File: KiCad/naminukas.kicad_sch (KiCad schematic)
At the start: 10 parts

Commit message: fix(pcb): better symbol for TPSM84A21MOJR
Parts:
- added U?: TPSM84A21MOJR, Texas_Instruments-MOJ0020A-0-0-*, symbol Buck (build-in caps):TPSM84A21MOJR
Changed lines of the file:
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@@
     (pin "Y2")
+  )
+  (symbol (lib_id "Buck (build-in caps):TPSM84A21MOJR") (at 31.75 139.7 0) (unit 1)
+    (in_bom yes) (on_board yes) (fields_autoplaced)
+    (property "Reference" "U?" (id 0) (at 52.07 132.08 0))
+    (property "Value" "TPSM84A21MOJR" (id 1) (at 52.07 134.62 0))
+    (property "Footprint" "Texas_Instruments-MOJ0020A-0-0-*" (id 2) (at 31.75 129.54 0)
+      (effects (font (size 1.27 1.27)) (justify left) hide)
+    )
+    (property "Datasheet" "https://www.ti.com/lit/ds/symlink/tpsm84a21.pdf?ts=1616475331887&ref_url=https%253A%252F%252Fwww.ti.com%252Fproduct%252FTPSM84A21%253FkeyMatch%253DTPSM84A21MOJR%2526tisearch%253Dsearch-everything%2526usecase%253DOPN" (id 3) (at 31.75 127 0)
+      (effects (font (size 1.27 1.27)) (justify left) hide)
+    )
+    (property "ambient temperature range high" "+85°C" (id 4) (at 31.75 124.46 0)
+      (effects (font (size 1.27 1.27)) (justify left) hide)
+    )
+    (property "ambient temperature range low" "-40°C" (id 5) (at 31.75 121.92 0)
+      (effects (font (size 1.27 1.27)) (justify left) hide)
+    )
+    (property "automotive" "No" (id 6) (at 31.75 119.38 0)
+      (effects (font (size 1.27 1.27)) (justify left) hide)
+    )
+    (property "category" "IC" (id 7) (at 31.75 116.84 0)
+      (effects (font (size 1.27 1.27)) (justify left) hide)
+    )
+    (property "device class L1" "Integrated Circuits (ICs)" (id 8) (at 31.75 114.3 0)
+      (effects (font (size 1.27 1.27)) (justify left) hide)
+    )
+    (property "device class L2" "Power Management ICs" (id 9) (at 31.75 111.76 0)
+      (effects (font (size 1.27 1.27)) (justify left) hide)
+    )
+    (property "device class L3" "Voltage Regulators - Switching" (id 10) (at 31.75 109.22 0)
+      (effects (font (size 1.27 1.27)) (justify left) hide)
+    )
+    (property "digikey description" "DC DC CONVERTER 0.55-1.35V" (id 11) (at 31.75 106.68 0)
+      (effects (font (size 1.27 1.27)) (justify left) hide)
+    )
+    (property "digikey part number" "296-48785-1-ND" (id 12) (at 31.75 104.14 0)
+      (effects (font (size 1.27 1.27)) (justify left) hide)
+    )
+    (property "height" "2.3mm" (id 13) (at 31.75 101.6 0)
+      (effects (font (size 1.27 1.27)) (justify left) hide)
+    )
+    (property "ipc land pattern name" "CAPAD1016W80L630D240" (id 14) (at 31.75 99.06 0)
+      (effects (font (size 1.27 1.27)) (justify left) hide)
+    )
+    (property "lead free" "Yes" (id 15) (at 31.75 96.52 0)
+      (effects (font (size 1.27 1.27)) (justify left) hide)
+    )
+    (property "library id" "cebd5fe4464742bf" (id 16) (at 31.75 93.98 0)
+      (effects (font (size 1.27 1.27)) (justify left) hide)
+    )
+    (property "manufacturer" "Texas Instruments" (id 17) (at 31.75 91.44 0)
+      (effects (font (size 1.27 1.27)) (justify left) hide)
+    )
+    (property "max duty cycle" "80%" (id 18) (at 31.75 88.9 0)
+      (effects (font (size 1.27 1.27)) (justify left) hide)
+    )
+    (property "max junction temp" "+125°C" (id 19) (at 31.75 86.36 0)
+      (effects (font (size 1.27 1.27)) (justify left) hide)
+    )
+    (property "max supply voltage" "14V" (id 20) (at 31.75 83.82 0)
+      (effects (font (size 1.27 1.27)) (justify left) hide)
+    )
+    (property "min supply voltage" "8V" (id 21) (at 31.75 81.28 0)
+      (effects (font (size 1.27 1.27)) (justify left) hide)
+    )
+    (property "mouser description" "8V to 14V, 0.508V to 1.35V Output, 10A Power Module with Integrated Input and Output Capacitors 20-QFM -40 to 85" (id 22) (at 31.75 78.74 0)
+      (effects (font (size 1.27 1.27)) (justify left) hide)
+    )
+    (property "mouser part number" "595-TPSM84A21MOJR" (id 23) (at 31.75 76.2 0)
+      (effects (font (size 1.27 1.27)) (justify left) hide)
+    )
+    (property "nominal supply current" "8mA" (id 24) (at 31.75 73.66 0)
+      (effects (font (size 1.27 1.27)) (justify left) hide)
+    )
+    (property "number of outputs" "1" (id 25) (at 31.75 71.12 0)
+      (effects (font (size 1.27 1.27)) (justify left) hide)
+    )
+    (property "output current" "10A" (id 26) (at 31.75 68.58 0)
+      (effects (font (size 1.27 1.27)) (justify left) hide)
+    )
+    (property "output type" "AdjustableProgrammable" (id 27) (at 31.75 66.04 0)
+      (effects (font (size 1.27 1.27)) (justify left) hide)
+    )
+    (property "output voltage" "0.55-1.35V" (id 28) (at 31.75 63.5 0)
+      (effects (font (size 1.27 1.27)) (justify left) hide)
+    )
+    (property "package" "QFM20" (id 29) (at 31.75 60.96 0)
+      (effects (font (size 1.27 1.27)) (justify left) hide)
+    )
+    (property "rohs" "Yes" (id 30) (at 31.75 58.42 0)
+      (effects (font (size 1.27 1.27)) (justify left) hide)
+    )
+    (property "switching frequency" "4MHz" (id 31) (at 31.75 55.88 0)
+      (effects (font (size 1.27 1.27)) (justify left) hide)
+    )
+    (property "temperature range high" "+85°C" (id 32) (at 31.75 53.34 0)
+      (effects (font (size 1.27 1.27)) (justify left) hide)
+    )
+    (property "temperature range low" "-40°C" (id 33) (at 31.75 50.8 0)
+      (effects (font (size 1.27 1.27)) (justify left) hide)
+    )
+    (pin "1")
+    (pin "10")
+    (pin "11")
+    (pin "12")
+    (pin "13")
+    (pin "14")
+    (pin "15")
+    (pin "16")
+    (pin "17")
+    (pin "18")
+    (pin "19")
+    (pin "2")
+    (pin "20")
+    (pin "3")
+    (pin "4")
+    (pin "5")
+    (pin "6")
+    (pin "7")
+    (pin "8")
+    (pin "9")
   )
   (symbol (lib_id "FPGA_Lattice:LFE5U-85F-6BG381x") (at 70.9676 73.7108 0) (unit 3)
@@
       (reference "IC?") (unit 1) (value "LSF0204DYZPR") (footprint "BGA12C50P3X4_144X194X50")
     )
+    (path "/66b1abfc-a54e-42e9-baa0-69e7c5971dd2"
+      (reference "U?") (unit 1) (value "TPSM84A21MOJR") (footprint "Texas_Instruments-MOJ0020A-0-0-*")
+    )
     (path "/f35b2073-882e-4ac0-9440-1e7208b06a2e"

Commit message: fix(pcb): better footprint for TPS84320RUQR
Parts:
- added U?: TPS84320RUQR, RUQ_47, symbol Buck converter:TPS84320RUQR
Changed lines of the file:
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@@
+    (pin "9")
+  )
+  (symbol (lib_id "Buck converter:TPS84320RUQR") (at 95.25 134.62 0) (unit 1)
+    (in_bom yes) (on_board yes) (fields_autoplaced)
+    (property "Reference" "U?" (id 0) (at 120.65 123.19 0)
+      (effects (font (size 1.524 1.524)))
+    )
+    (property "Value" "TPS84320RUQR" (id 1) (at 120.65 127 0)
+      (effects (font (size 1.524 1.524)))
+    )
+    (property "Footprint" "RUQ_47" (id 2) (at 120.65 128.524 0)
+      (effects (font (size 1.524 1.524)) hide)
+    )
+    (property "Datasheet" "" (id 3) (at 95.25 134.62 0)
+      (effects (font (size 1.524 1.524)))
+    )
+    (pin "1")
+    (pin "10")
+    (pin "11")
+    (pin "12")
+    (pin "13")
+    (pin "14")
+    (pin "15")
+    (pin "16")
+    (pin "17")
+    (pin "18")
+    (pin "19")
+    (pin "2")
+    (pin "20")
+    (pin "21")
+    (pin "22")
+    (pin "23")
+    (pin "24")
+    (pin "25")
+    (pin "26")
+    (pin "27")
+    (pin "28")
+    (pin "29")
+    (pin "3")
+    (pin "30")
+    (pin "31")
+    (pin "32")
+    (pin "33")
+    (pin "34")
+    (pin "35")
+    (pin "36")
+    (pin "37")
+    (pin "38")
+    (pin "39")
+    (pin "4")
+    (pin "40")
+    (pin "41")
+    (pin "42")
+    (pin "43")
+    (pin "44")
+    (pin "45")
+    (pin "46")
+    (pin "47")
+    (pin "5")
+    (pin "6")
+    (pin "7")
+    (pin "8")
     (pin "9")
   )
@@
       (reference "U?") (unit 1) (value "TPSM84A21MOJR") (footprint "Texas_Instruments-MOJ0020A-0-0-*")
     )
+    (path "/70e86428-6b27-40a3-ae68-cb62b9e219e9"
+      (reference "U?") (unit 1) (value "TPS84320RUQR") (footprint "RUQ_47")
+    )
     (path "/f35b2073-882e-4ac0-9440-1e7208b06a2e"

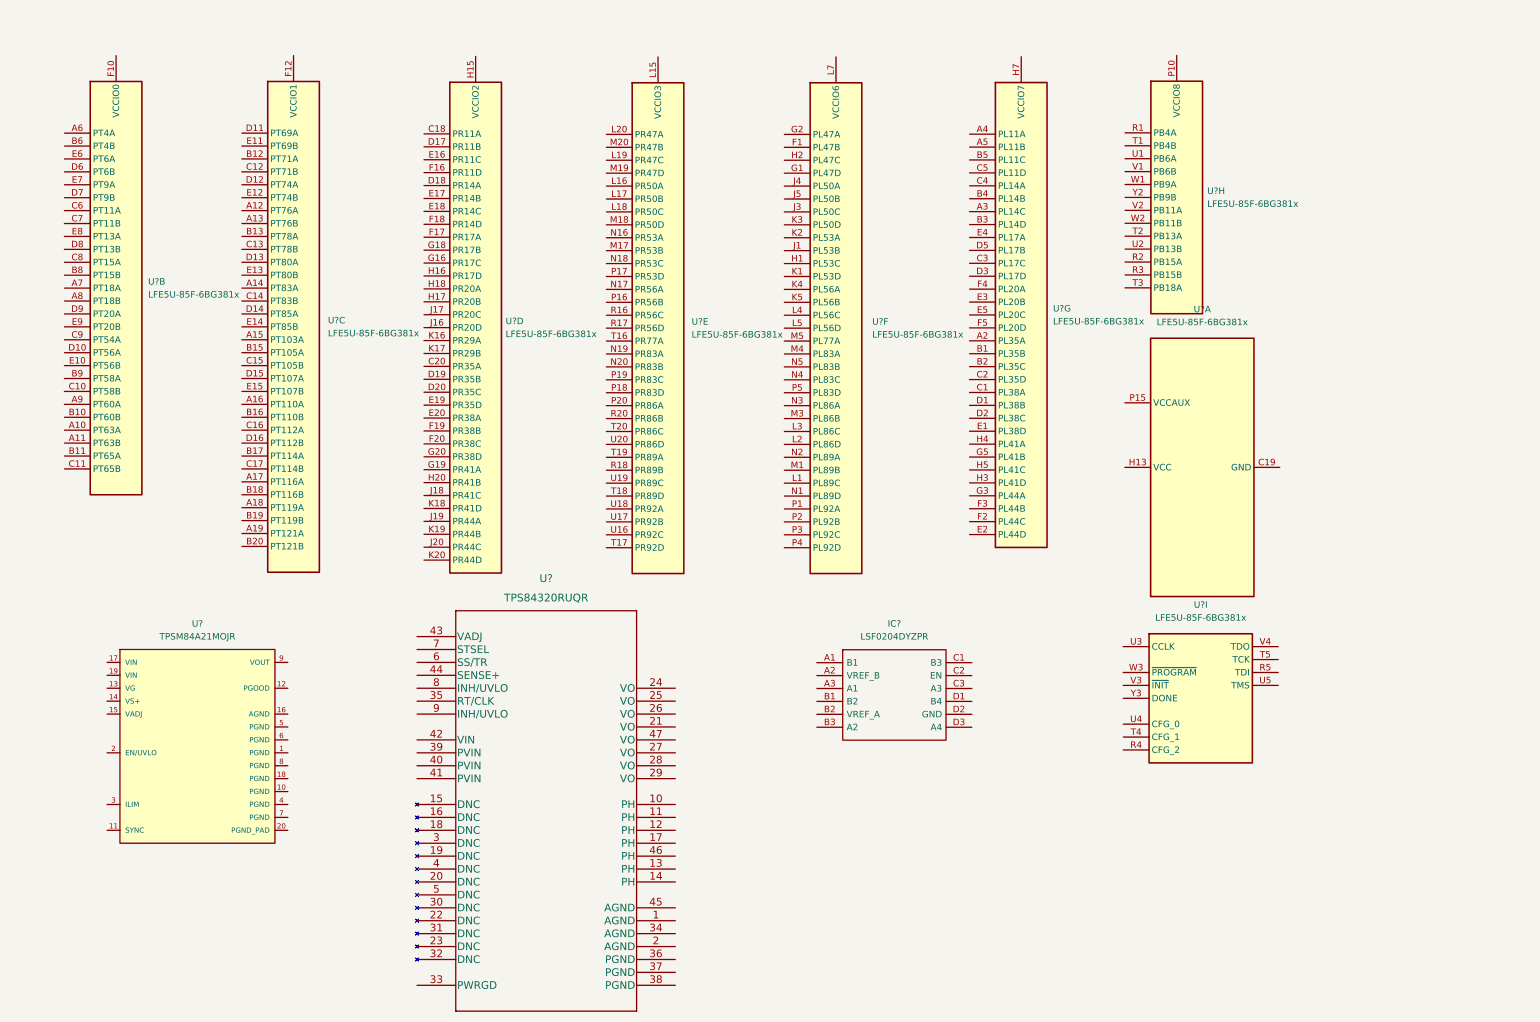
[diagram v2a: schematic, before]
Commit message: feat(pcb): add symbol/footprint for LFE5U-85F-6MG285C
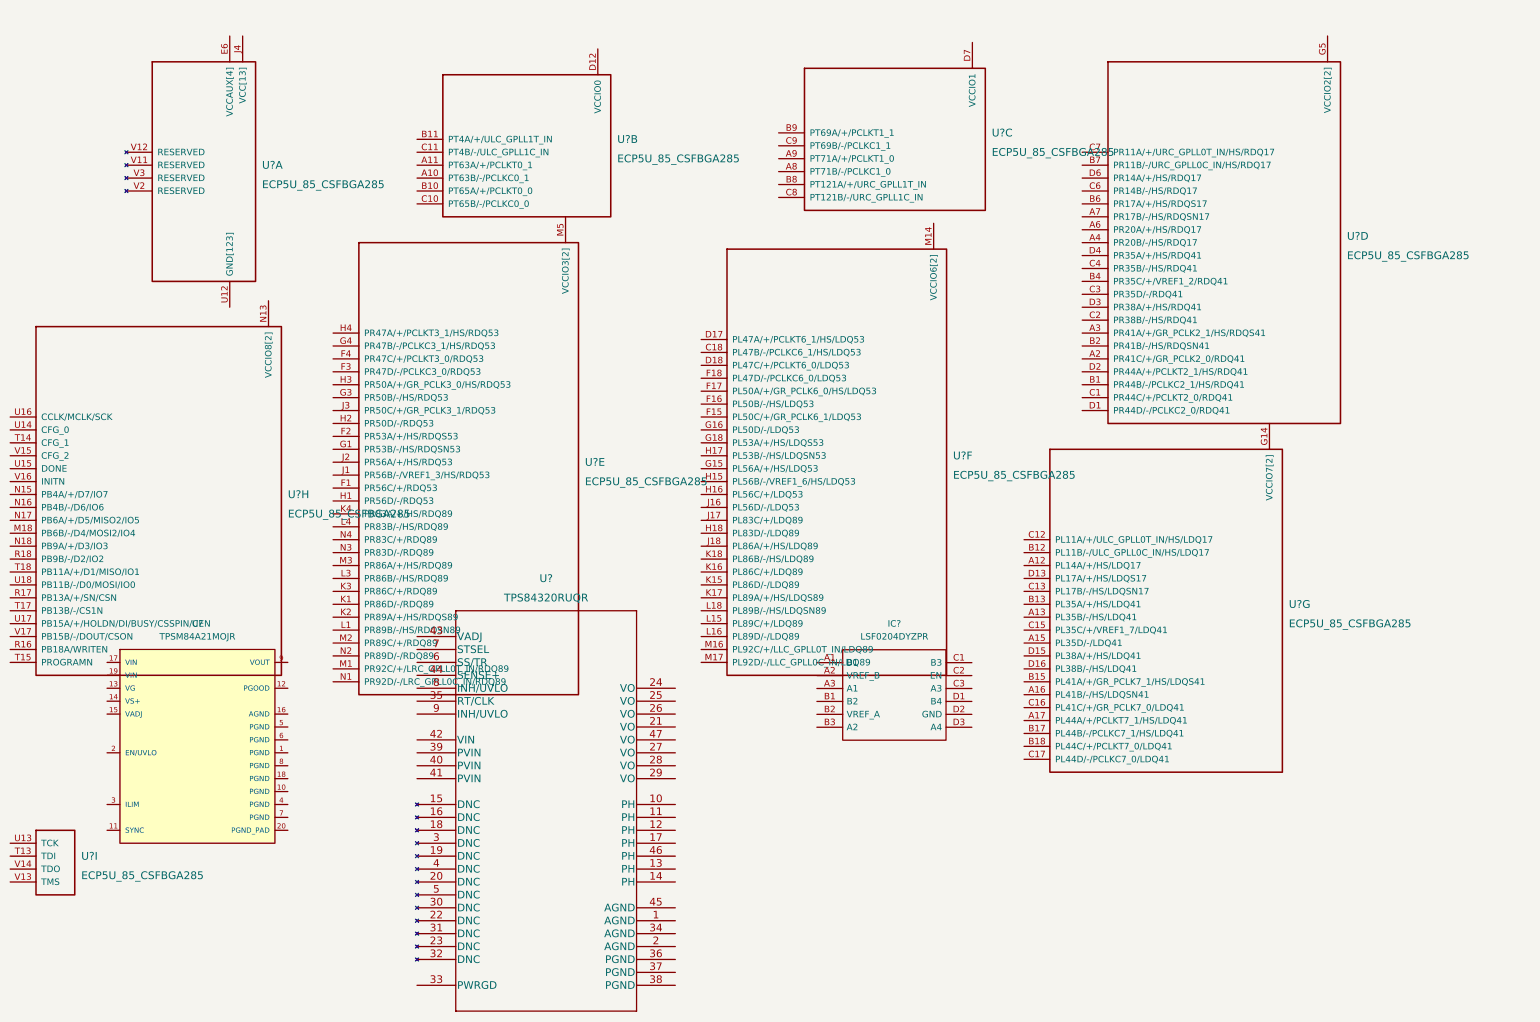
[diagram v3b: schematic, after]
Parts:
- removed U? (x9): LFE5U-85F-6BG381x, Package_BGA:Lattice_caBGA-381_17.0x17.0mm_Layout20x20_P0.8mm_Ball0.4mm_Pad0.4mm_NSMD, symbol FPGA_Lattice:LFE5U-85F-6BG381x
- added U? (x8): ECP5U_85_CSFBGA285, symbol ECP5:ECP5U_85_CSFBGA285
- added U?: ECP5U_85_CSFBGA285, ECP5:BGA285C50P18X18_1000X1000X130, symbol ECP5:ECP5U_85_CSFBGA285
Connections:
- new net: U?.G14 (VCCIO7[2]), U?.H14 (VCCIO7[2])
- new net: U?.M14 (VCCIO6[2]), U?.N14 (VCCIO6[2])
- new net: U?.M5 (VCCIO3[2]), U?.N5 (VCCIO3[2])
- new net: U?.N13 (VCCIO8[2]), U?.P14 (VCCIO8[2])
- new net: U?.B16 (GND[123]), U?.B3 (GND[123]), U?.E10 (GND[123]), U?.E11 (GND[123]), U?.E12 (GND[123]), U?.E14 (GND[123]), U?.E5 (GND[123]), U?.E7 (GND[123]), U?.E8 (GND[123]), U?.E9 (GND[123]), U?.F10 (GND[123]), U?.F11 (GND[123]), U?.F12 (GND[123]), U?.F13 (GND[123]), U?.F14 (GND[123]), U?.F5 (GND[123]), U?.F6 (GND[123]), U?.F7 (GND[123]), U?.F8 (GND[123]), U?.F9 (GND[123]), U?.G10 (GND[123]), U?.G11 (GND[123]), U?.G12 (GND[123]), U?.G13 (GND[123]), U?.G17 (GND[123]), U?.G2 (GND[123]), U?.G6 (GND[123]), U?.G7 (GND[123]), U?.G8 (GND[123]), U?.G9 (GND[123]), U?.H10 (GND[123]), U?.H11 (GND[123]), U?.H12 (GND[123]), U?.H13 (GND[123]), U?.H6 (GND[123]), U?.H7 (GND[123]), U?.H8 (GND[123]), U?.H9 (GND[123]), U?.J10 (GND[123]), U?.J11 (GND[123]), U?.J12 (GND[123]), U?.J13 (GND[123]), U?.J6 (GND[123]), U?.J7 (GND[123]), U?.J8 (GND[123]), U?.J9 (GND[123]), U?.K10 (GND[123]), U?.K11 (GND[123]), U?.K12 (GND[123]), U?.K13 (GND[123]), U?.K14 (GND[123]), U?.K5 (GND[123]), U?.K6 (GND[123]), U?.K7 (GND[123]), U?.K8 (GND[123]), U?.K9 (GND[123]), U?.L10 (GND[123]), U?.L11 (GND[123]), U?.L12 (GND[123]), U?.L13 (GND[123]), U?.L14 (GND[123]), U?.L17 (GND[123]), U?.L2 (GND[123]), U?.L5 (GND[123]), U?.L6 (GND[123]), U?.L7 (GND[123]), U?.L8 (GND[123]), U?.L9 (GND[123]), U?.M10 (GND[123]), U?.M11 (GND[123]), U?.M12 (GND[123]), U?.M13 (GND[123]), U?.M6 (GND[123]), U?.M7 (GND[123]), U?.M8 (GND[123]), U?.M9 (GND[123]), U?.N10 (GND[123]), U?.N11 (GND[123]), U?.N12 (GND[123]), U?.N7 (GND[123]), U?.N8 (GND[123]), U?.N9 (GND[123]), U?.P10 (GND[123]), U?.P12 (GND[123]), U?.P5 (GND[123]), U?.P6 (GND[123]), U?.P8 (GND[123]), U?.R1 (GND[123]), U?.R10 (GND[123]), U?.R2 (GND[123]), U?.R3 (GND[123]), U?.T1 (GND[123]), U?.T10 (GND[123]), U?.T11 (GND[123]), U?.T12 (GND[123]), U?.T16 (GND[123]), U?.T2 (GND[123]), U?.T3 (GND[123]), U?.T4 (GND[123]), U?.T5 (GND[123]), U?.T6 (GND[123]), U?.T7 (GND[123]), U?.T8 (GND[123]), U?.T9 (GND[123]), U?.U1 (GND[123]), U?.U10 (GND[123]), U?.U11 (GND[123]), U?.U12 (GND[123]), U?.U2 (GND[123]), U?.U3 (GND[123]), U?.U4 (GND[123]), U?.U5 (GND[123]), U?.U6 (GND[123]), U?.U7 (GND[123]), U?.U8 (GND[123]), U?.U9 (GND[123]), U?.V10 (GND[123]), U?.V4 (GND[123]), U?.V5 (GND[123]), U?.V6 (GND[123]), U?.V7 (GND[123]), U?.V8 (GND[123]), U?.V9 (GND[123])
- new net: U?.D10 (VCC[13]), U?.D11 (VCC[13]), U?.D8 (VCC[13]), U?.D9 (VCC[13]), U?.J14 (VCC[13]), U?.J15 (VCC[13]), U?.J4 (VCC[13]), U?.J5 (VCC[13]), U?.M15 (VCC[13]), U?.M4 (VCC[13]), U?.P11 (VCC[13]), U?.P7 (VCC[13]), U?.P9 (VCC[13])
- new net: U?.E13 (VCCAUX[4]), U?.E6 (VCCAUX[4]), U?.N6 (VCCAUX[4]), U?.P13 (VCCAUX[4])
- new net: U?.G5 (VCCIO2[2]), U?.H5 (VCCIO2[2])

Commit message: feat(pcb): add SPI flash W25Q128JVPIQ
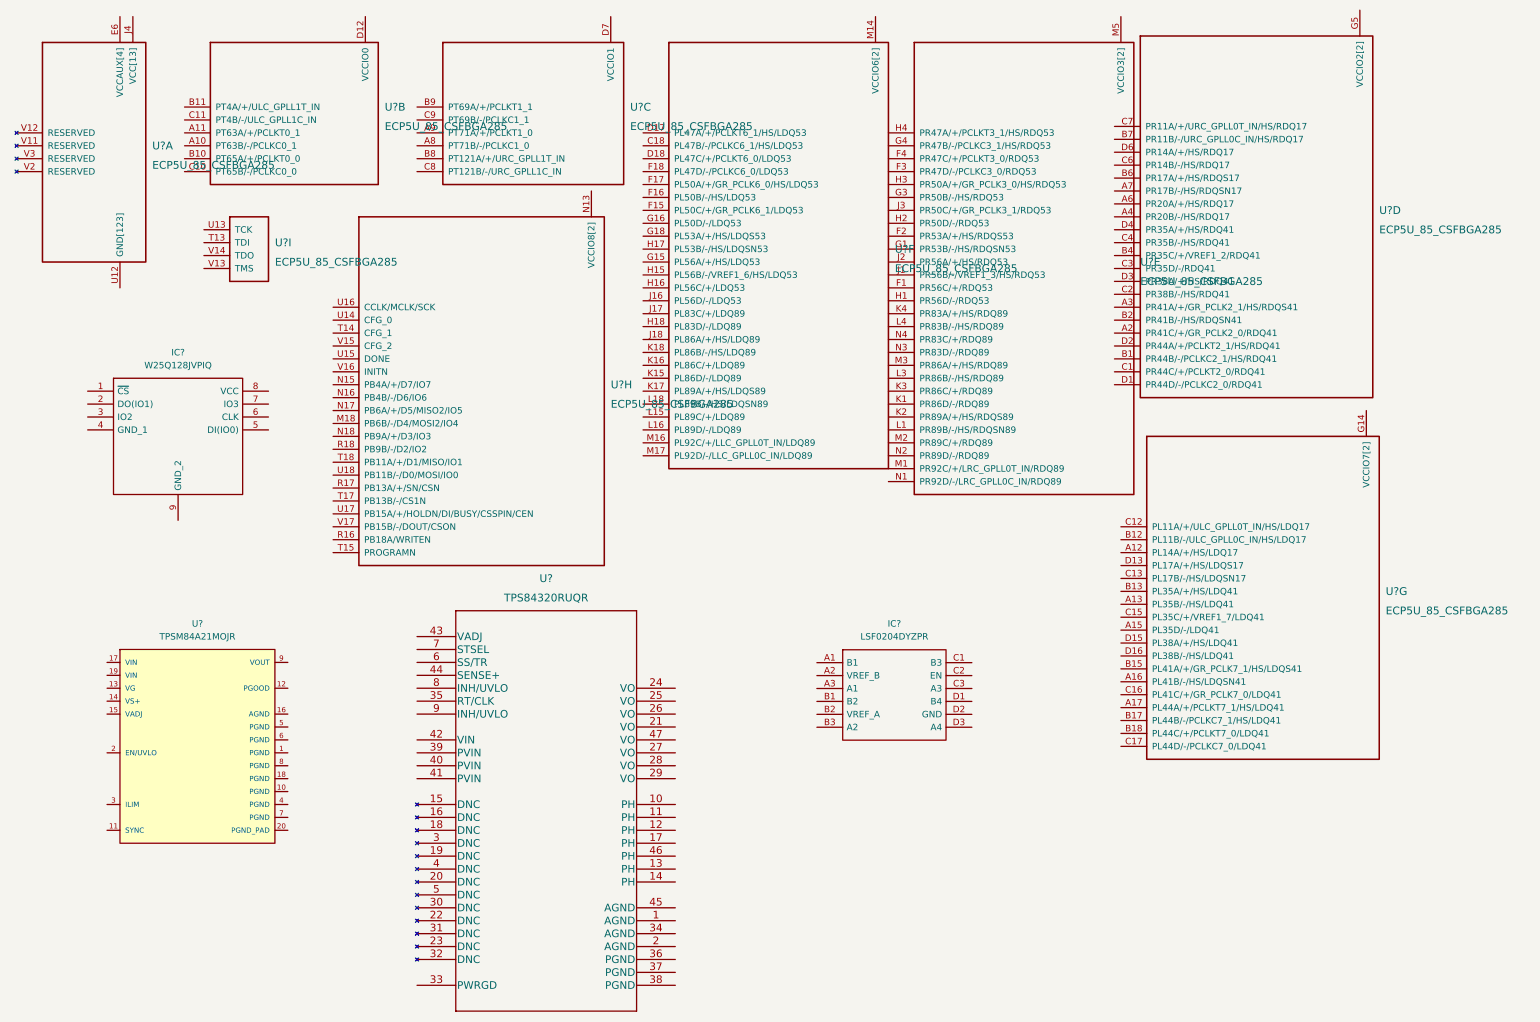
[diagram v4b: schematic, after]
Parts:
- added IC?: W25Q128JVPIQ, SON127P800X600X80-9N-D, symbol SPI Flash:W25Q128JVPIQ
- U?: footprint (none) -> ECP5:BGA285C50P18X18_1000X1000X130
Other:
- moved on the sheet: U?A, U?B, U?C, U?D, U?E, U?F, U?G, U?H, U?I
